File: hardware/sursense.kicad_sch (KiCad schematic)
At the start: 9 parts, among them J1 USB_C_Receptacle, J2 GC9A01, J3 Microphone, SW1 SW_Push, SW2 SW_Push, SW3 EC11, U1 ESP32-S3-WROOM-1, U2 MAX98357A

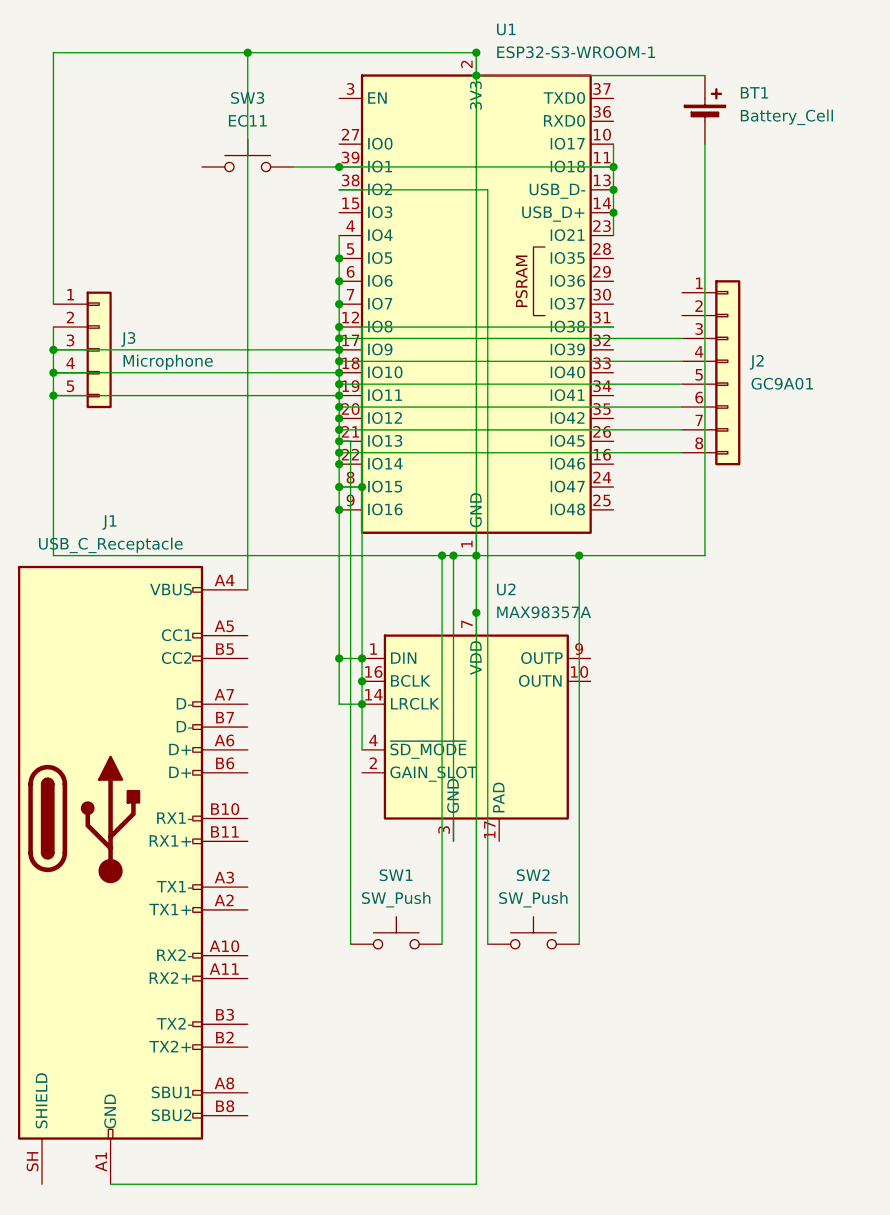
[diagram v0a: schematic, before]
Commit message: Fix schematic shorts by replacing wires with net labels
The wired version collapsed 57 wires into 3 nets. A single vertical
wire ran down the left pin column of U1 acting as a busbar, so every
horizontal run terminating on it was welded to the same net, with
battery + tied to battery -.

Replaced all wires and junctions with net labels placed on the pins.
Now 20 nets, largest is GND, and every net matches the README pin map:
mic on IO4/5/6, amp on IO7/15/16 with shutdown on IO38, display on
IO8-IO12 and IO14, encoder on IO17/18, buttons on IO13 and IO2.

Also drop cad/__pycache__ from the repo.

Co-Authored-By: Claude Opus 5 <noreply@anthropic.com>
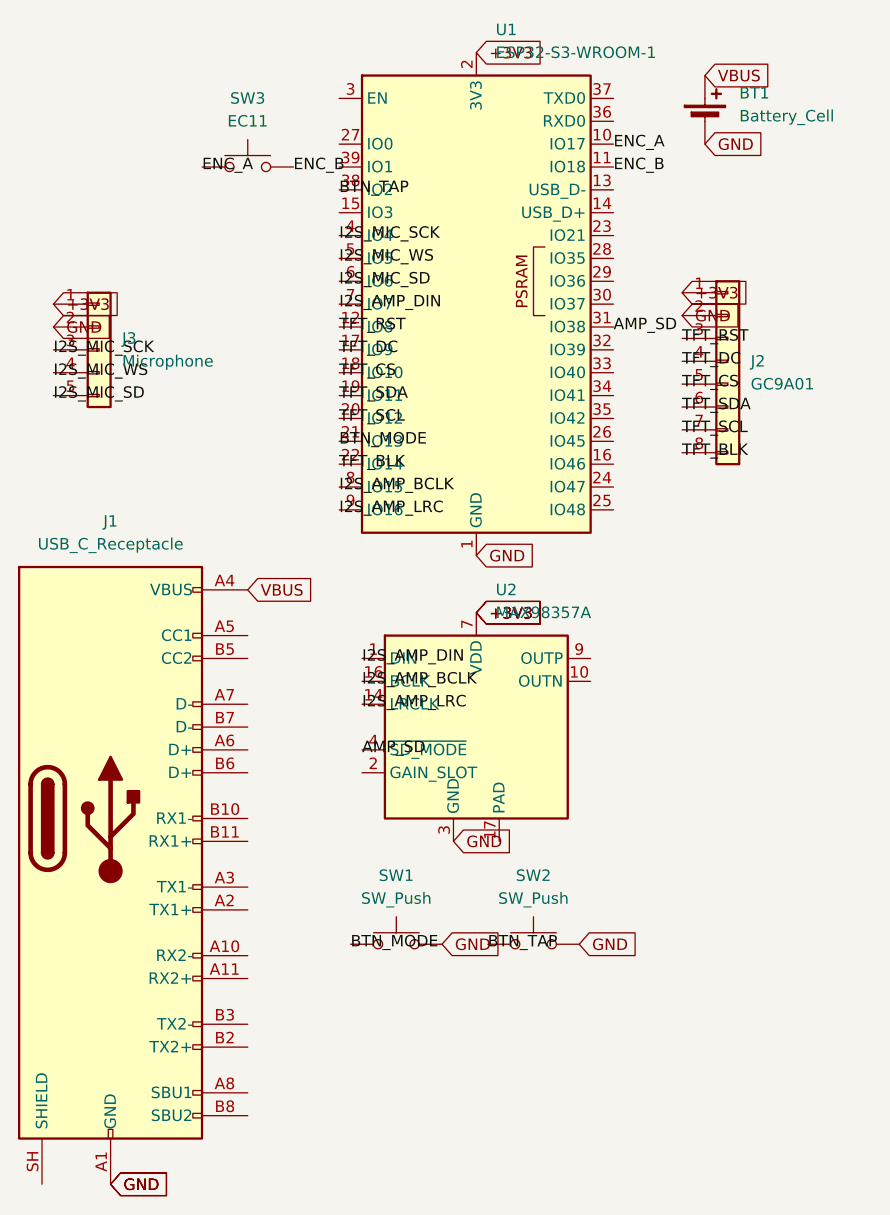
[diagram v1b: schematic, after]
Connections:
- net BTN_TAP: now reaches SW2.1, U1.38 (IO2)
- net +3V3: now reaches J2.1 (Pin_1)
- net +3V3: now also J3.1 (Pin_1), U1.2 (3V3), U2.7 (VDD), U2.8 (VDD)
- net GND: now reaches J2.2 (Pin_2)
- net GND: now also BT1.2 (-), J1.A1 (GND), J1.A12 (GND), J1.B1 (GND), J1.B12 (GND), J3.2 (Pin_2), SW1.2, SW2.2, U1.1 (GND), U1.40 (GND), U1.41 (GND), U2.11 (GND), U2.15 (GND), U2.3 (GND)
- net ENC_A: now reaches SW3.1
- net ENC_A: now also U1.10 (IO17)
- new net AMP_SD: U1.31 (IO38), U2.4 (~{SD_MODE})
- new net BTN_MODE: SW1.1, U1.21 (IO13)
- new net ENC_B: SW3.2, U1.11 (IO18)
- new net I2S_AMP_BCLK: U1.8 (IO15), U2.16 (BCLK)
- new net I2S_AMP_DIN: U1.7 (IO7), U2.1 (DIN)
- new net I2S_AMP_LRC: U1.9 (IO16), U2.14 (LRCLK)
- new net I2S_MIC_SCK: J3.3 (Pin_3), U1.4 (IO4)
- new net I2S_MIC_SD: J3.5 (Pin_5), U1.6 (IO6)
- new net I2S_MIC_WS: J3.4 (Pin_4), U1.5 (IO5)
- new net TFT_BLK: J2.8 (Pin_8), U1.22 (IO14)
- new net TFT_CS: J2.5 (Pin_5), U1.18 (IO10)
- new net TFT_DC: J2.4 (Pin_4), U1.17 (IO9)
- new net TFT_RST: J2.3 (Pin_3), U1.12 (IO8)
- new net TFT_SCL: J2.7 (Pin_7), U1.20 (IO12)
- new net TFT_SDA: J2.6 (Pin_6), U1.19 (IO11)
- new net VBUS: BT1.1 (+), J1.A4 (VBUS), J1.A9 (VBUS), J1.B4 (VBUS), J1.B9 (VBUS)
- now unconnected: U1.13 (USB_D-), U1.14 (USB_D+), U1.23 (IO21), U1.39 (IO1)
